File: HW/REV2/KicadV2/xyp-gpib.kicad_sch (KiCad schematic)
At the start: 25 parts, among them J1 USB_C_Receptacle_USB2.0, SW1 SW_Push, U1 ATmega32U4-MU, Y1 CX2016DB16000D0WZRC1

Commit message: Update to KiCAD 8.0.4 and add Digi-Key part numbers.
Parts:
- C1: Digi-Key_PN (none) -> 1276-1244-1-ND
- C2, C3, C4: Digi-Key_PN (none) -> CC0603ZRY5V9BB104
- C5, C6: Digi-Key_PN (none) -> 1292-1549-1-ND
- C7: value 1u -> 1uF; Digi-Key_PN (none) -> 311-1446-1-ND
- D1, D2: Digi-Key_PN (none) -> 732-4985-1-ND
- FID1, FID2, ISP1: now left out of the parts list
- GPIB1: value 112-024-113R001 -> 112-024-113L001; Digi-Key_PN (none) -> 1024PMA-ND; Manufacturer_Part_Number 112-024-113R001 -> 111-024-113L001; Mouser Part Number 636-112-024-113R001 -> 636-111-024-113L001; Mouser Price/Stock https://www.mouser.co.uk/ProductDetail/NorComp/112-024-113R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 -> https://www.mouser.com/ProductDetail/NorComp/111-024-113L00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
- J1: Digi-Key_PN (none) -> 52-USB-CB16HTBTRCT-ND
- R1: Digi-Key_PN (none) -> 311-10.0KHRCT-ND
- R2, R3: Digi-Key_PN (none) -> 311-22.0HRCT-ND
- R4, R6: Digi-Key_PN (none) -> 311-470HRCT-ND
- R5: Digi-Key_PN (none) -> 311-100KHRCT-ND
- R7, R8: Digi-Key_PN (none) -> 311-5.10KHRCT-ND; MPN (none) -> RC0603FR-075K1L
- SW1: Digi-Key_PN (none) -> CKN12329-1-ND
- U1: Digi-Key_PN (none) -> ATMEGA32U4-MU-ND
- Y1: Digi-Key_PN (none) -> 478-CX2016DB16000D0WZRC1CT-ND
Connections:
- no-connect marks 0 -> 5
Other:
- title: (none) -> UsbGpib

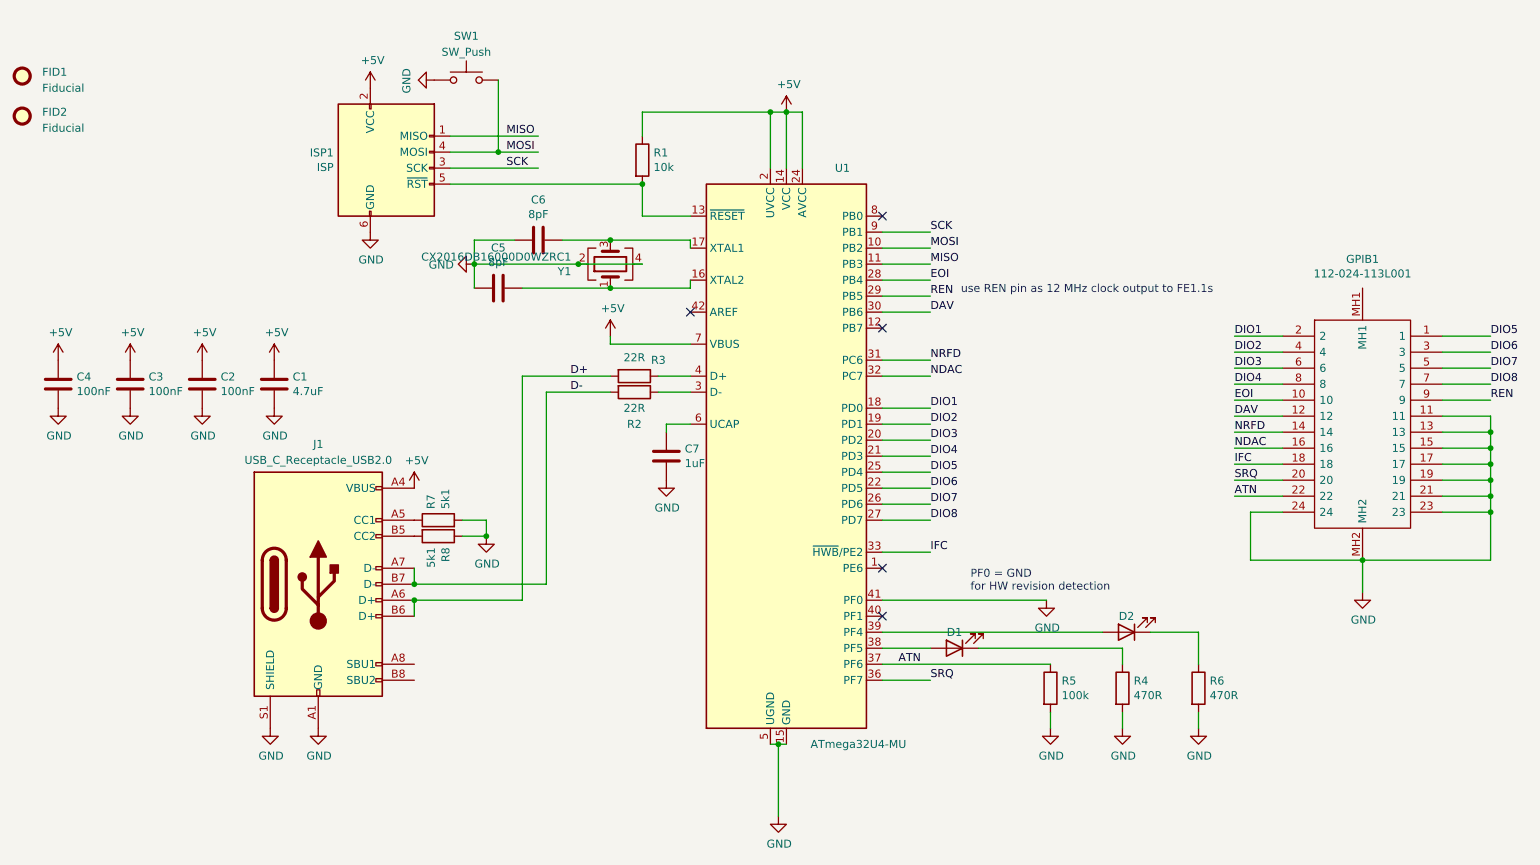
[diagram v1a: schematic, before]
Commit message: Fix pinout and pin 1 orientation of GPIB connector.
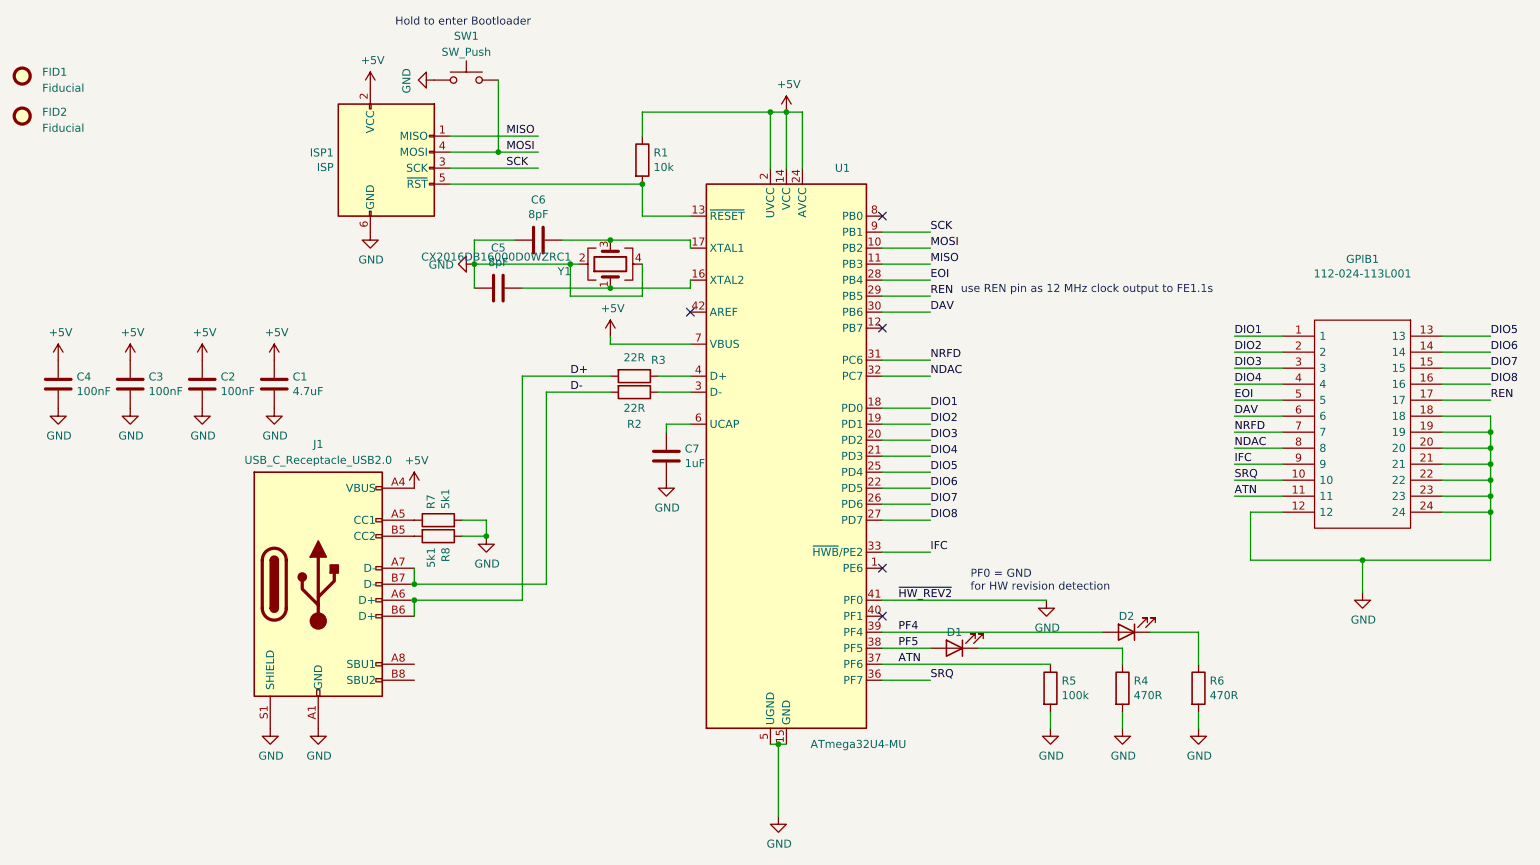
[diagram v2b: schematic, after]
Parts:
- GPIB1: footprint gpib:112024113R001 -> ac125a_dtmf:111-024-113L001; symbol conn-gpib:112-024-113R001 -> ac125a_dtmf:111-024-113L001
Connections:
- net ATN: now also GPIB1.11; no longer GPIB1.22
- net DAV: now also GPIB1.6; no longer GPIB1.12
- net DIO1: now also GPIB1.1; no longer GPIB1.2
- net DIO2: now also GPIB1.2; no longer GPIB1.4
- net DIO3: now also GPIB1.3; no longer GPIB1.6
- net DIO4: now also GPIB1.4; no longer GPIB1.8
- net DIO5: now also GPIB1.13; no longer GPIB1.1
- net DIO6: now also GPIB1.14; no longer GPIB1.3
- net DIO7: now also GPIB1.15; no longer GPIB1.5
- net DIO8: now also GPIB1.16; no longer GPIB1.7
- net EOI: now also GPIB1.5; no longer GPIB1.10
- net GND: now also GPIB1.12, GPIB1.18, GPIB1.20, GPIB1.22; no longer GPIB1.11, GPIB1.13, GPIB1.15, GPIB1.17, GPIB1.MH2
- net IFC: now also GPIB1.9; no longer GPIB1.18
- net NDAC: now also GPIB1.8; no longer GPIB1.16
- net NRFD: now also GPIB1.7; no longer GPIB1.14
- net REN: now also GPIB1.17; no longer GPIB1.9
- net SRQ: now also GPIB1.10; no longer GPIB1.20
- net PF5: now reaches D1.2 (A), U1.38 (PF5)
- net PF4: now reaches D2.2 (A), U1.39 (PF4)
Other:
- note added: "Hold to enter Bootloader"
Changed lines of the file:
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@@
 	(title_block
 		(title "UsbGpib")
-		(date "2024-08-03")
-		(rev "2")
+		(date "2024-08-18")
+		(rev "2.1")
 	)
 	(junction
@@
 	)
 	(junction
+		(at 106.68 69.85)
+		(diameter 0)
+		(color 0 0 0 0)
+	)
+	(junction
 		(at 252.73 99.06)
 		(diameter 0)
@@
 	(junction
 		(at 232.41 116.84)
-		(diameter 0)
-		(color 0 0 0 0)
-	)
-	(junction
-		(at 107.95 69.85)
 		(diameter 0)
 		(color 0 0 0 0)
@@
 	(wire
 		(pts
-			(xy 107.95 69.85) (xy 91.44 69.85)
+			(xy 107.95 69.85) (xy 106.68 69.85)
 		)
 		(stroke
@@
 	(wire
 		(pts
+			(xy 106.68 69.85) (xy 91.44 69.85)
+		)
+		(stroke
+			(width 0)
+			(type default)
+		)
+	)
+	(wire
+		(pts
 			(xy 87.63 54.61) (xy 101.6 54.61)
 		)
@@
 	(wire
 		(pts
+			(xy 106.68 74.93) (xy 106.68 69.85)
+		)
+		(stroke
+			(width 0)
+			(type default)
+		)
+	)
+	(wire
+		(pts
 			(xy 99.06 73.66) (xy 113.03 73.66)
 		)
@@
 	(wire
 		(pts
+			(xy 118.11 74.93) (xy 106.68 74.93)
+		)
+		(stroke
+			(width 0)
+			(type default)
+		)
+	)
+	(wire
+		(pts
 			(xy 118.11 45.72) (xy 138.43 45.72)
 		)
@@
 	(wire
 		(pts
-			(xy 118.11 69.85) (xy 107.95 69.85)
+			(xy 118.11 69.85) (xy 118.11 74.93)
 		)
 		(stroke
@@
 			(width 0)
 			(type default)
+		)
+	)
+	(text "Hold to enter Bootloader"
+		(exclude_from_sim no)
+		(at 89.662 31.496 0)
+		(effects
+			(font
+				(size 1.27 1.27)
+			)
 		)
 	)
@@
 		)
 	)
+	(label "~{HW_REV2}"
+		(at 158.75 123.19 0)
+		(fields_autoplaced yes)
+		(effects
+			(font
+				(size 1.27 1.27)
+			)
+			(justify left bottom)
+		)
+	)
 	(label "REN"
 		(at 252.73 91.44 0)
@@
 		)
 	)
+	(label "PF4"
+		(at 158.75 128.27 0)
+		(fields_autoplaced yes)
+		(effects
+			(font
+				(size 1.27 1.27)
+			)
+			(justify left bottom)
+		)
+	)
 	(label "DIO5"
 		(at 163.83 102.87 0)
@@
 		)
 	)
+	(label "PF5"
+		(at 158.75 130.81 0)
+		(fields_autoplaced yes)
+		(effects
+			(font
+				(size 1.27 1.27)
+			)
+			(justify left bottom)
+		)
+	)
 	(label "NRFD"
 		(at 163.83 85.09 0)
@@
 	)
 	(symbol
-		(lib_id "conn-gpib:112-024-113R001")
-		(at 232.41 73.66 90)
-		(mirror x)
+		(lib_id "ac125a_dtmf:111-024-113L001")
+		(at 232.41 73.66 270)
 		(unit 1)
 		(exclude_from_sim no)
@@
 			)
 		)
-		(property "Footprint" "gpib:112024113R001"
-			(at 224.79 113.03 0)
+		(property "Footprint" "ac125a_dtmf:111-024-113L001"
+			(at 240.03 113.03 0)
 			(effects
 				(font
@@
 		)
 		(property "Datasheet" "https://de.aliexpress.com/item/1005005636771892.html?spm=a2g0o.productlist.main.1.6e3872e5tUudMA&algo_pvid=3c848d5c-bbef-4a4a-b8ad-041402717ac1&algo_exp_id=3c848d5c-bbef-4a4a-b8ad-041402717ac1-0&pdp_npi=4%40dis%21EUR%211.21%211.21%21%21%219.17%21%21%40211b801616979974338462951e1d1e%2112000033838675279%21sea%21DE%210%21AB&curPageLogUid=Fdxeh4JTGSVM"
-			(at 227.33 113.03 0)
+			(at 237.49 113.03 0)
 			(effects
 				(font
@@
 		)
 		(property "Description" "I/O Connectors 24P Centronics male R/A dip solder"
-			(at 229.87 113.03 0)
+			(at 234.95 113.03 0)
 			(effects
 				(font
@@
 		)
 		(property "Manufacturer_Name" "NorComp"
-			(at 234.95 113.03 0)
+			(at 229.87 113.03 0)
 			(effects
 				(font
@@
 		)
 		(property "Manufacturer_Part_Number" "111-024-113L001"
-			(at 237.49 113.03 0)
+			(at 227.33 113.03 0)
 			(effects
 				(font
@@
 		)
 		(property "Mouser Part Number" "636-111-024-113L001"
-			(at 240.03 113.03 0)
+			(at 224.79 113.03 0)
 			(effects
 				(font
@@
 		)
 		(property "Mouser Price/Stock" "https://www.mouser.com/ProductDetail/NorComp/111-024-113L001?qs=IGgAdOvCTsTzuqCRtmjabw%3D%3D"
-			(at 242.57 113.03 0)
+			(at 222.25 113.03 0)
 			(effects
 				(font
@@
 		)
 		(property "Arrow Part Number" ""
-			(at 245.11 113.03 0)
+			(at 219.71 113.03 0)
 			(effects
 				(font
@@
 		)
 		(property "Arrow Price/Stock" ""
-			(at 247.65 113.03 0)
+			(at 217.17 113.03 0)
 			(effects
 				(font
@@
 		(pin "9"
 		)
-		(pin "MH1"
-		)
-		(pin "MH2"
-		)
 		(instances
